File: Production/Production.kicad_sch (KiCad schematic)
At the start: 30 parts, among them IC1 MAX3323EEPE+, J1 530480510, J2 530480410, J3 USB4085-GF-A_REVB, U1 BD33FC0FP-E2, U2 ADR02AUJZ-REEL7, U3 ATSAMD21G18A-AUT, Y1 32.768, 12.5pF

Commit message: Started work on production board v1
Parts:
- removed S4: ZERO, PVA1EEH21.2NV2:PVA1EEH212NV2, symbol PVA1EEH21_2NV2:PVA1EEH21.2NV2
- added C13: 20uF,60V+, Capacitor_SMD:C_0805_2012Metric, symbol Device:C
- C1, C2, C3, C5, C6, C7, C8: footprint Capacitor_SMD:C_1812_4532Metric_Pad1.57x3.40mm_HandSolder -> Capacitor_SMD:C_0805_2012Metric
- C4: value 0.33uF,60V+ -> 20uF,60V+; footprint Capacitor_SMD:C_1812_4532Metric_Pad1.57x3.40mm_HandSolder -> Capacitor_SMD:C_0805_2012Metric
- D1, D2: footprint Diode_SMD:D_1812_4532Metric_Pad1.30x3.40mm_HandSolder -> Diode_SMD:D_1206_3216Metric
- D3, D4: footprint LED_THT:LED_D5.0mm -> LED_SMD:LED_0805_2012Metric
- IC1: footprint MAX3323EEPE+:DIP794W56P254L1918H457Q16N -> Package_SO:TSSOP-16_4.4x5mm_P0.65mm
- J1: footprint 530480510:CON_530480510_MOL -> Connector_Molex_2:Molex_PicoBlade_53048-0510_1x05_P1.25mm_Horizontal
- J2: footprint 530480410:CON_530480410_MOL -> Connector_Molex:Molex_PicoBlade_53048-0410_1x04_P1.25mm_Horizontal
- R1, R2, R3, R4, R5, R8: footprint Resistor_SMD:R_1206_3216Metric_Pad1.30x1.75mm_HandSolder -> Resistor_SMD:R_0805_2012Metric
- U3: footprint digikey-footprints:TQFP-48_7x7mm -> Package_QFP:TQFP-48_7x7mm_P0.5mm
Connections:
- net RSTB2 is gone; now on net RST: S1.B2
- net SETB2 is gone; now on net SETBTN: S2.B2
- net SOFTB2 is gone; now on net SOFTBTN: S3.B2
- net +3V3: now also C13.2
- net GND: now also C13.1
- net RST: no longer S1.A1
- net SETBTN: no longer S2.A1
- net SOFTBTN: no longer S3.A1
- net PA04: no longer names the net of U3.9 (PA04)
- net PA05: no longer names the net of U3.10 (PA05)
- net PA06: no longer names the net of U3.11 (PA06)
- net PA08 renamed OLED_RST
- net PB08: no longer names the net of U3.7 (PB08)
- net PB09: no longer names the net of U3.8 (PB09)
- net RSTB1: no longer names the net of S1.B1
- net SETB1: no longer names the net of S2.B1
- net SOFTB1: no longer names the net of S3.B1
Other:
- moved on the sheet: S1, S2, S3

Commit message: Solid layout, could be better
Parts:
- removed S1: RESET, PVA1EEH21.2NV2:PVA1EEH212NV2, symbol PVA1EEH21_2NV2:PVA1EEH21.2NV2
- removed S2: SET, PVA1EEH21.2NV2:PVA1EEH212NV2, symbol PVA1EEH21_2NV2:PVA1EEH21.2NV2
- removed S3: SOFT, PVA1EEH21.2NV2:PVA1EEH212NV2, symbol PVA1EEH21_2NV2:PVA1EEH21.2NV2
- added RESET1: B3U-1000P, Button_Switch_SMD:SW_SPST_B3U-1000P, symbol dk_Tactile-Switches:B3U-1000P
- added SET1, SOFT1: TS01-66-73-BK-160-D, TS01-66-73-BK-160-D:TS016673BK160D, symbol TS01-66-73-BK-160-D:TS01-66-73-BK-160-D
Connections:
- net GND: now also RESET1.1, SET1.3 (COM_1), SOFT1.3 (COM_1)
- net RST: now also RESET1.2
- net SETBTN: now also SET1.1 (NO_1)
- net SOFTBTN: now also SOFT1.1 (NO_1)

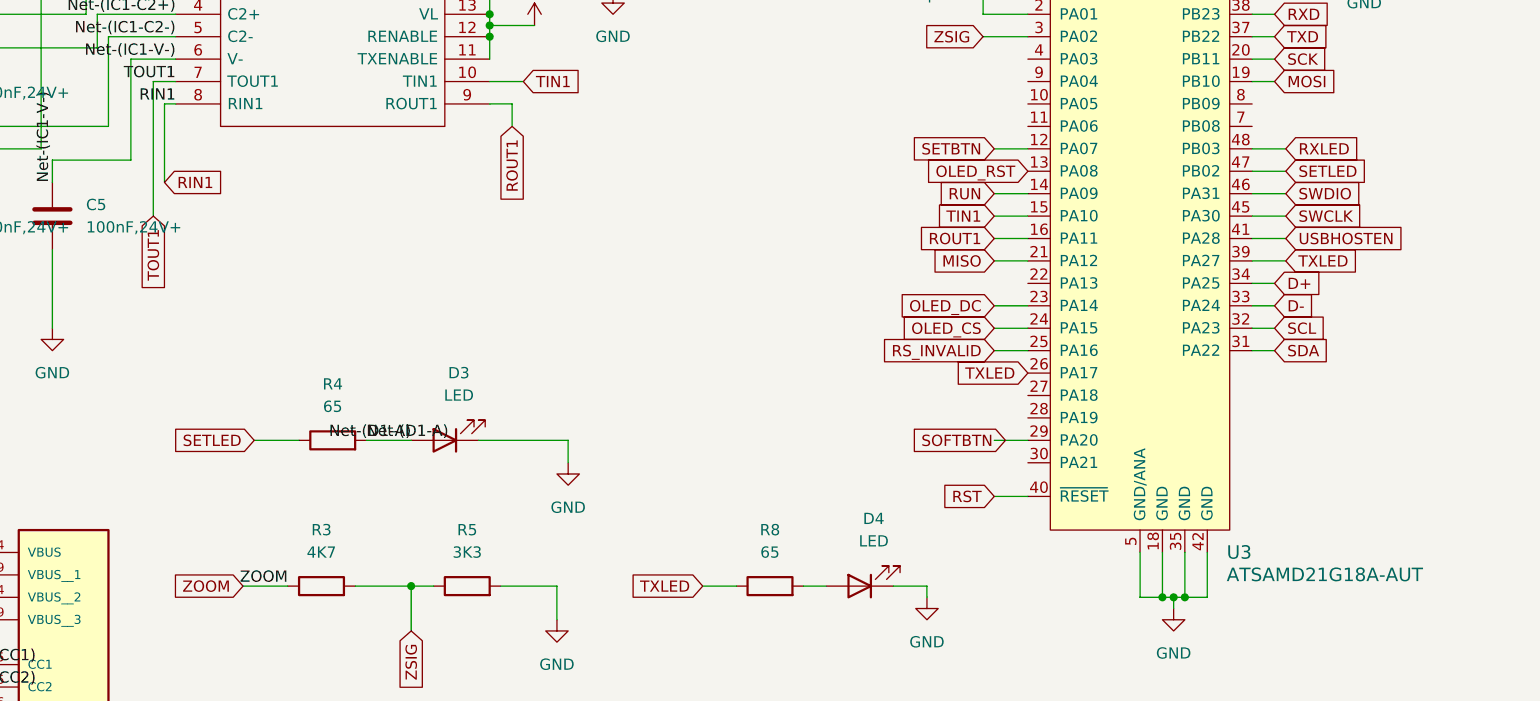
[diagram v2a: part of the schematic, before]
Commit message: Combined TXLED and SETLED
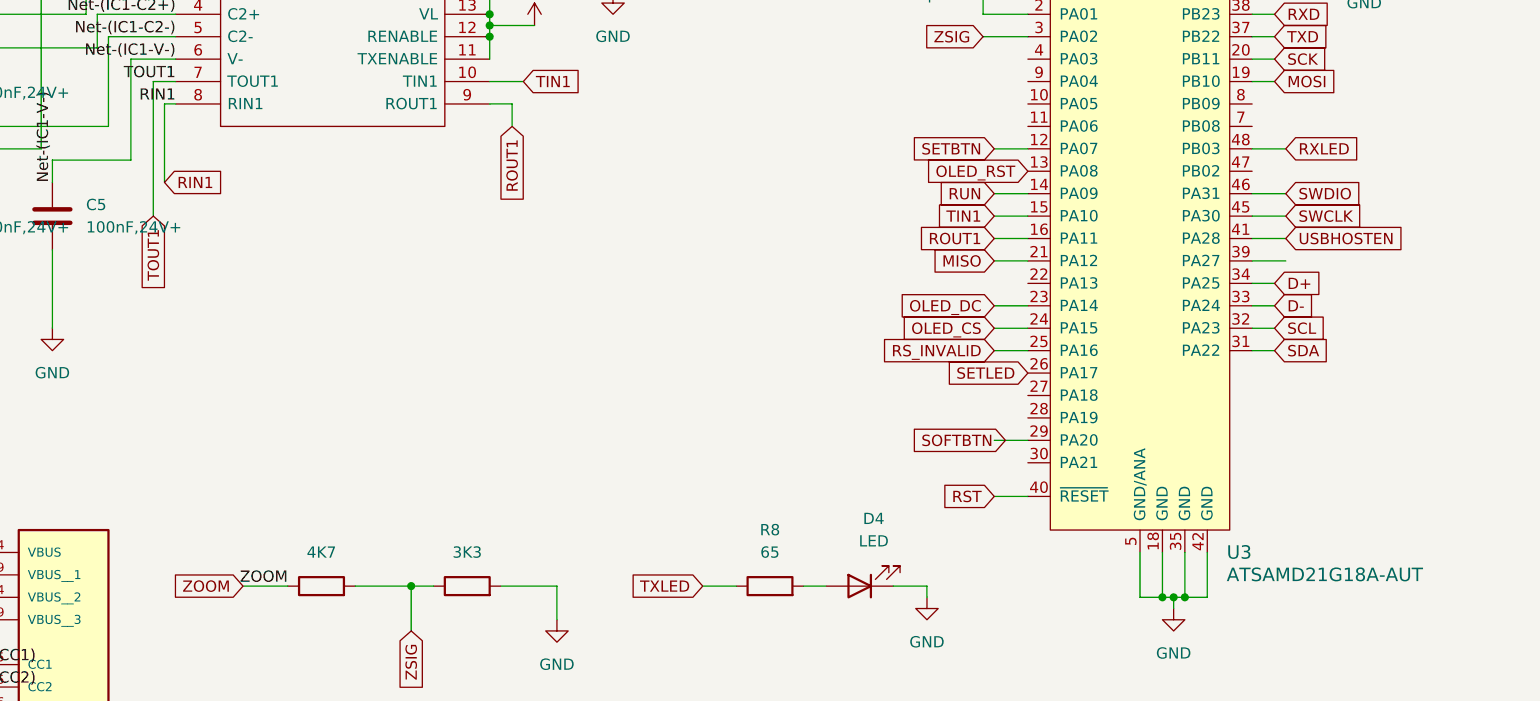
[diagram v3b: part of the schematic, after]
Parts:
- removed D3: LED, LED_SMD:LED_0805_2012Metric, symbol Device:LED
- removed R4: 65, Resistor_SMD:R_0805_2012Metric, symbol Device:R
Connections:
- net SETLED: now also U3.26 (PA17); no longer U3.47 (PB02)
- net TXLED: no longer U3.26 (PA17), U3.39 (PA27)

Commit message: I layout
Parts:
- C1, C13, C2, C3, C4, C5, C6, C7, C8: footprint Capacitor_SMD:C_0805_2012Metric -> Capacitor_SMD:C_0504_1310Metric
- J2: footprint Connector_Molex:Molex_PicoBlade_53048-0410_1x04_P1.25mm_Horizontal -> Connector_Molex_2:Molex_PicoBlade_53048-0410_1x04_P1.25mm_Horizontal
- R1, R2, R3, R5, R8: footprint Resistor_SMD:R_0805_2012Metric -> Resistor_SMD:R_0603_1608Metric
- U2: footprint Package_TO_SOT_SMD:TSOT-23-5_HandSoldering -> Package_TO_SOT_SMD:TSOT-23-5
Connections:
- net RS_INVALID is gone; now on net OLED_DC: U3.25 (PA16)
- net TXLED is gone; now on net SETLED: R8.1
- net OLED_CS: now also U3.23 (PA14); no longer U3.24 (PA15)
- net OLED_DC: no longer U3.23 (PA14)
- net OLED_RST: now also U3.24 (PA15); no longer U3.13 (PA08)
- net RUN: now also U3.47 (PB02); no longer U3.14 (PA09)
- net SETBTN: now also U3.29 (PA20); no longer U3.12 (PA07)
- net SOFTBTN: now also U3.12 (PA07); no longer U3.29 (PA20)
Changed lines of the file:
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@@
 	(wire
 		(pts
-			(xy 227.33 99.06) (xy 231.14 99.06)
-		)
-		(stroke
-			(width 0)
-			(type default)
-		)
-	)
-	(wire
-		(pts
 			(xy 105.41 165.1) (xy 107.95 165.1)
 		)
@@
 		)
 	)
-	(global_label "TXLED"
+	(global_label "MOSI"
 		(shape input)
-		(at 194.31 143.51 180)
+		(at 259.08 86.36 0)
 		(fields_autoplaced yes)
 		(effects
@@
 				(size 1.27 1.27)
 			)
-			(justify right)
+			(justify left)
 		)
 		(property "Intersheetrefs" "${INTERSHEET_REFS}"
-			(at 185.7006 143.51 0)
+			(at 266.6614 86.36 0)
 			(effects
 				(font
 					(size 1.27 1.27)
 				)
-				(justify right)
+				(justify left)
 				(hide yes)
 			)
 		)
 	)
-	(global_label "MOSI"
+	(global_label "ZREF"
 		(shape input)
-		(at 259.08 86.36 0)
+		(at 266.7 22.86 90)
 		(fields_autoplaced yes)
 		(effects
@@
 		)
 		(property "Intersheetrefs" "${INTERSHEET_REFS}"
-			(at 266.6614 86.36 0)
+			(at 266.7 15.1577 90)
 			(effects
 				(font
@@
 		)
 	)
-	(global_label "ZREF"
+	(global_label "TXD"
 		(shape input)
-		(at 266.7 22.86 90)
+		(at 259.08 81.28 0)
 		(fields_autoplaced yes)
 		(effects
@@
 		)
 		(property "Intersheetrefs" "${INTERSHEET_REFS}"
-			(at 266.7 15.1577 90)
+			(at 265.5123 81.28 0)
 			(effects
 				(font
@@
 		)
 	)
-	(global_label "TXD"
+	(global_label "SETLED"
 		(shape input)
-		(at 259.08 81.28 0)
+		(at 194.31 143.51 180)
 		(fields_autoplaced yes)
 		(effects
@@
 				(size 1.27 1.27)
 			)
-			(justify left)
+			(justify right)
 		)
 		(property "Intersheetrefs" "${INTERSHEET_REFS}"
-			(at 265.5123 81.28 0)
+			(at 184.5516 143.51 0)
 			(effects
 				(font
 					(size 1.27 1.27)
 				)
-				(justify left)
+				(justify right)
 				(hide yes)
 			)
@@
 	(global_label "OLED_RST"
 		(shape input)
-		(at 231.14 96.52 180)
+		(at 227.33 114.3 180)
 		(fields_autoplaced yes)
 		(effects
@@
 		)
 		(property "Intersheetrefs" "${INTERSHEET_REFS}"
-			(at 218.9625 96.52 0)
+			(at 215.1525 114.3 0)
 			(effects
 				(font
@@
 	(global_label "SOFTBTN"
 		(shape input)
-		(at 228.6 127 180)
+		(at 227.33 93.98 180)
 		(fields_autoplaced yes)
 		(effects
@@
 		)
 		(property "Intersheetrefs" "${INTERSHEET_REFS}"
-			(at 217.4505 127 0)
+			(at 216.1805 93.98 0)
 			(effects
 				(font
@@
 	(global_label "SETBTN"
 		(shape input)
-		(at 227.33 93.98 180)
+		(at 227.33 127 180)
 		(fields_autoplaced yes)
 		(effects
@@
 		)
 		(property "Intersheetrefs" "${INTERSHEET_REFS}"
-			(at 217.4506 93.98 0)
-			(effects
-				(font
-					(size 1.27 1.27)
-				)
-				(justify right)
-				(hide yes)
-			)
-		)
-	)
-	(global_label "RS_INVALID"
-		(shape input)
-		(at 227.33 116.84 180)
-		(fields_autoplaced yes)
-		(effects
-			(font
-				(size 1.27 1.27)
-			)
-			(justify right)
-		)
-		(property "Intersheetrefs" "${INTERSHEET_REFS}"
-			(at 213.8823 116.84 0)
-			(effects
-				(font
-					(size 1.27 1.27)
-				)
-				(justify right)
-				(hide yes)
-			)
-		)
-	)
-	(global_label "RUN"
-		(shape input)
-		(at 227.33 99.06 180)
-		(fields_autoplaced yes)
-		(effects
-			(font
-				(size 1.27 1.27)
-			)
-			(justify right)
-		)
-		(property "Intersheetrefs" "${INTERSHEET_REFS}"
-			(at 220.4138 99.06 0)
+			(at 217.4506 127 0)
 			(effects
 				(font
@@
 		)
 	)
+	(global_label "RUN"
+		(shape input)
+		(at 256.54 96.52 0)
+		(fields_autoplaced yes)
+		(effects
+			(font
+				(size 1.27 1.27)
+			)
+			(justify left)
+		)
+		(property "Intersheetrefs" "${INTERSHEET_REFS}"
+			(at 263.4562 96.52 0)
+			(effects
+				(font
+					(size 1.27 1.27)
+				)
+				(justify left)
+				(hide yes)
+			)
+		)
+	)
 	(global_label "TIN1"
 		(shape input)
@@
 	(global_label "OLED_DC"
 		(shape input)
-		(at 227.33 111.76 180)
+		(at 227.33 116.84 180)
 		(fields_autoplaced yes)
 		(effects
@@
 		)
 		(property "Intersheetrefs" "${INTERSHEET_REFS}"
-			(at 216.0596 111.76 0)
+			(at 216.0596 116.84 0)
 			(effects
 				(font
@@
 	(global_label "OLED_CS"
 		(shape input)
-		(at 227.33 114.3 180)
+		(at 227.33 111.76 180)
 		(fields_autoplaced yes)
 		(effects
@@
 		)
 		(property "Intersheetrefs" "${INTERSHEET_REFS}"
-			(at 216.1201 114.3 0)
+			(at 216.1201 111.76 0)
 			(effects
 				(font
@@
 			)
 		)
-		(property "Footprint" "Capacitor_SMD:C_0805_2012Metric"
+		(property "Footprint" "Capacitor_SMD:C_0504_1310Metric"
 			(at 270.2052 69.85 0)
 			(effects
@@
 			)
 		)
-		(property "Footprint" "Package_TO_SOT_SMD:TSOT-23-5_HandSoldering"
+		(property "Footprint" "Package_TO_SOT_SMD:TSOT-23-5"
 			(at 199.39 27.94 0)
 			(effects
@@
 			)
 		)
-		(property "Footprint" "Capacitor_SMD:C_0805_2012Metric"
+		(property "Footprint" "Capacitor_SMD:C_0504_1310Metric"
 			(at 108.9152 90.17 0)
 			(effects
@@
 			)
 		)
-		(property "Footprint" "Capacitor_SMD:C_0805_2012Metric"
+		(property "Footprint" "Capacitor_SMD:C_0504_1310Metric"
 			(at 118.4148 38.1 0)
 			(effects
@@
 			)
 		)
-		(property "Footprint" "Resistor_SMD:R_0805_2012Metric"
+		(property "Footprint" "Resistor_SMD:R_0603_1608Metric"
 			(at 104.14 156.718 90)
 			(effects
@@
 			)
 		)
-		(property "Footprint" "Capacitor_SMD:C_0805_2012Metric"
+		(property "Footprint" "Capacitor_SMD:C_0504_1310Metric"
 			(at 174.2948 34.29 0)
 			(effects
@@
 			)
 		)
-		(property "Footprint" "Resistor_SMD:R_0805_2012Metric"
+		(property "Footprint" "Resistor_SMD:R_0603_1608Metric"
 			(at 104.14 154.178 90)
 			(effects
@@
 			)
 		)
-		(property "Footprint" "Resistor_SMD:R_0805_2012Metric"
+		(property "Footprint" "Resistor_SMD:R_0603_1608Metric"
 			(at 201.93 145.288 90)
 			(effects
@@
 			)
 		)
-		(property "Footprint" "Capacitor_SMD:C_0805_2012Metric"
+		(property "Footprint" "Capacitor_SMD:C_0504_1310Metric"
 			(at 121.6152 105.41 0)
 			(effects
@@
 			)
 		)
-		(property "Footprint" "Capacitor_SMD:C_0805_2012Metric"
+		(property "Footprint" "Capacitor_SMD:C_0504_1310Metric"
 			(at 108.9152 77.47 0)
 			(effects
@@
 			)
 		)
-		(property "Footprint" "Resistor_SMD:R_0805_2012Metric"
+		(property "Footprint" "Resistor_SMD:R_0603_1608Metric"
 			(at 151.13 145.288 90)
 			(effects
@@
 			)
 		)
-		(property "Footprint" "Resistor_SMD:R_0805_2012Metric"
+		(property "Footprint" "Resistor_SMD:R_0603_1608Metric"
 			(at 167.64 145.288 90)
 			(effects
@@
 			)
 		)
-		(property "Footprint" "Capacitor_SMD:C_0805_2012Metric"
+		(property "Footprint" "Capacitor_SMD:C_0504_1310Metric"
 			(at 223.52 63.8048 0)
 			(effects
@@
 			)
 		)
-		(property "Footprint" "Capacitor_SMD:C_0805_2012Metric"
+		(property "Footprint" "Capacitor_SMD:C_0504_1310Metric"
 			(at 223.52 68.8848 0)
 			(effects
@@
 			)
 		)
-		(property "Footprint" "Connector_Molex:Molex_PicoBlade_53048-0410_1x04_P1.25mm_Horizontal"
+		(property "Footprint" "Connector_Molex_2:Molex_PicoBlade_53048-0410_1x04_P1.25mm_Horizontal"
 			(at 54.61 81.28 0)
 			(effects
@@
 			)
 		)
-		(property "Footprint" "Capacitor_SMD:C_0805_2012Metric"
+		(property "Footprint" "Capacitor_SMD:C_0504_1310Metric"
 			(at 108.9152 105.41 0)
 			(effects

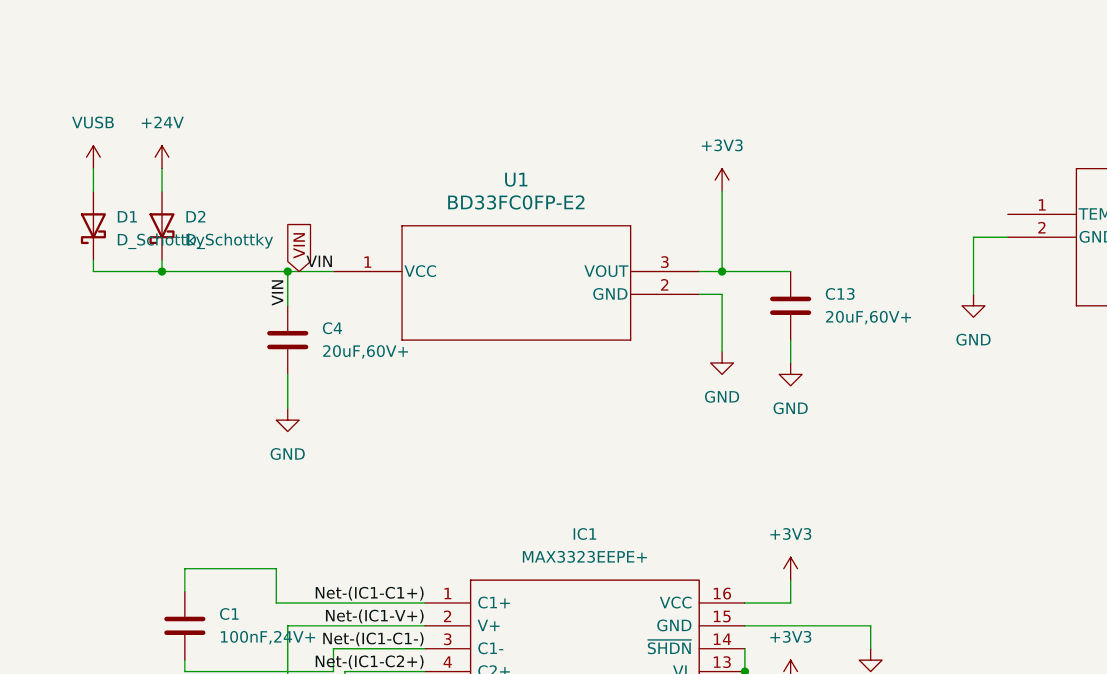
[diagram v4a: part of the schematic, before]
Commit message: Changing power regulator
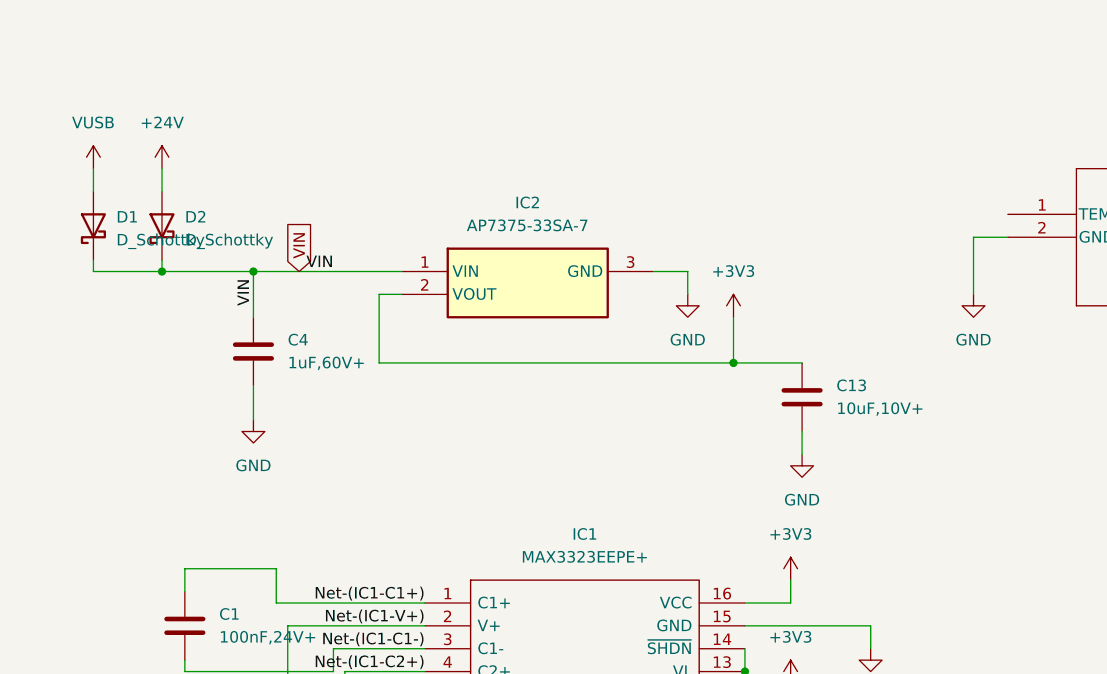
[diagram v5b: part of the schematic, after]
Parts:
- removed U1: BD33FC0FP-E2, Package_TO_SOT_SMD:TO-252-3_TabPin2, symbol 2024-05-14_22-26-41:BD433M5FP-CE2
- added IC2: AP7375-33SA-7, AP7375-33SA-7:SOT96P240X110-3N, symbol AP7375-33SA-7:AP7375-33SA-7
- C13: value 20uF,60V+ -> 10uF,10V+
- C4: value 20uF,60V+ -> 1uF,60V+
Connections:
- net +3V3: now also IC2.2 (VOUT)
- net GND: now also IC2.3 (GND)
- net VIN: now also IC2.1 (VIN)
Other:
- moved on the sheet: C13, C4
